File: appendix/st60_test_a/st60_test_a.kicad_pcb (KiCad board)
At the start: 2 copper layers, 55 x 10 mm, 4 parts, among them J1 Conn_01x02, J2 POGOPIN-E21160-ASB-2PIN

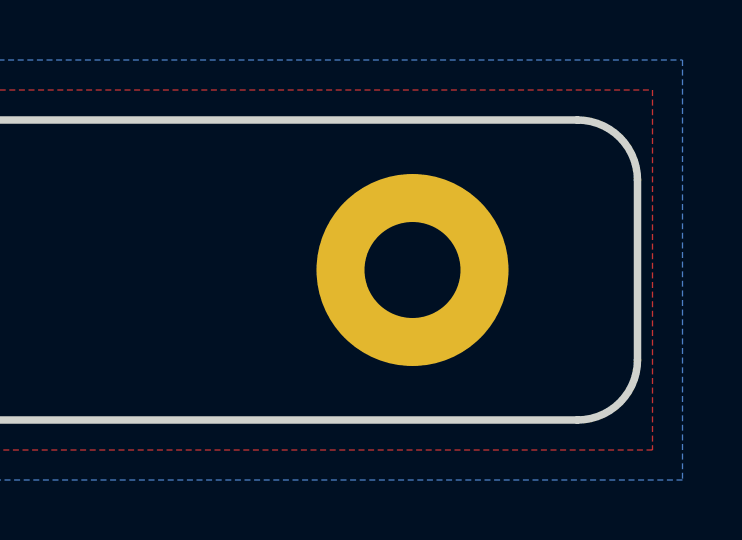
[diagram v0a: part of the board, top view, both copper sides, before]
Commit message: [Fix] Fix st60_test_a mountinghole position
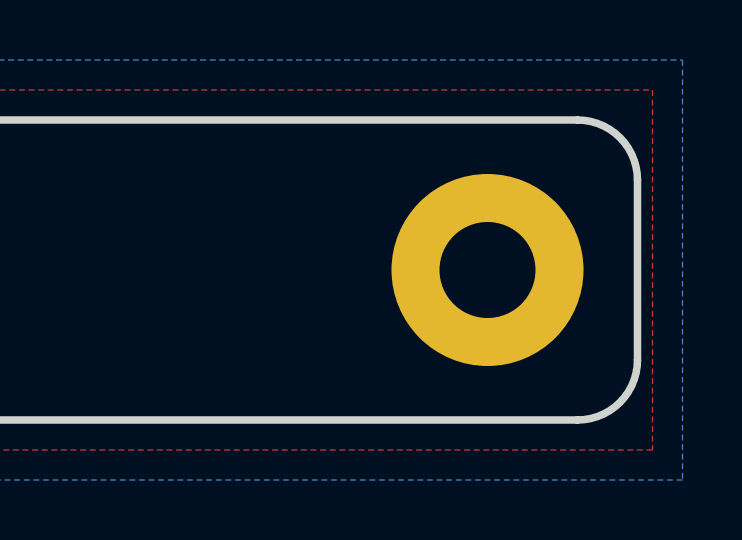
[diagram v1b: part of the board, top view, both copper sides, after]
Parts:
- moved REF** 2.50 mm to (177.5, 61.0)
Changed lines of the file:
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@@
   )
   (footprint "MountingHole:MountingHole_3.2mm_M3_Pad" (layer "F.Cu")
-    (at 175 61)
+    (at 177.5 61)
     (descr "Mounting Hole 3.2mm, M3")
     (tags "mounting hole 3.2mm m3")
